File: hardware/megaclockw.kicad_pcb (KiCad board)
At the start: 2 copper layers, 26.8 x 65.5 mm, 3 parts, among them J1 Conn_01x08_Female, U1 74HC245

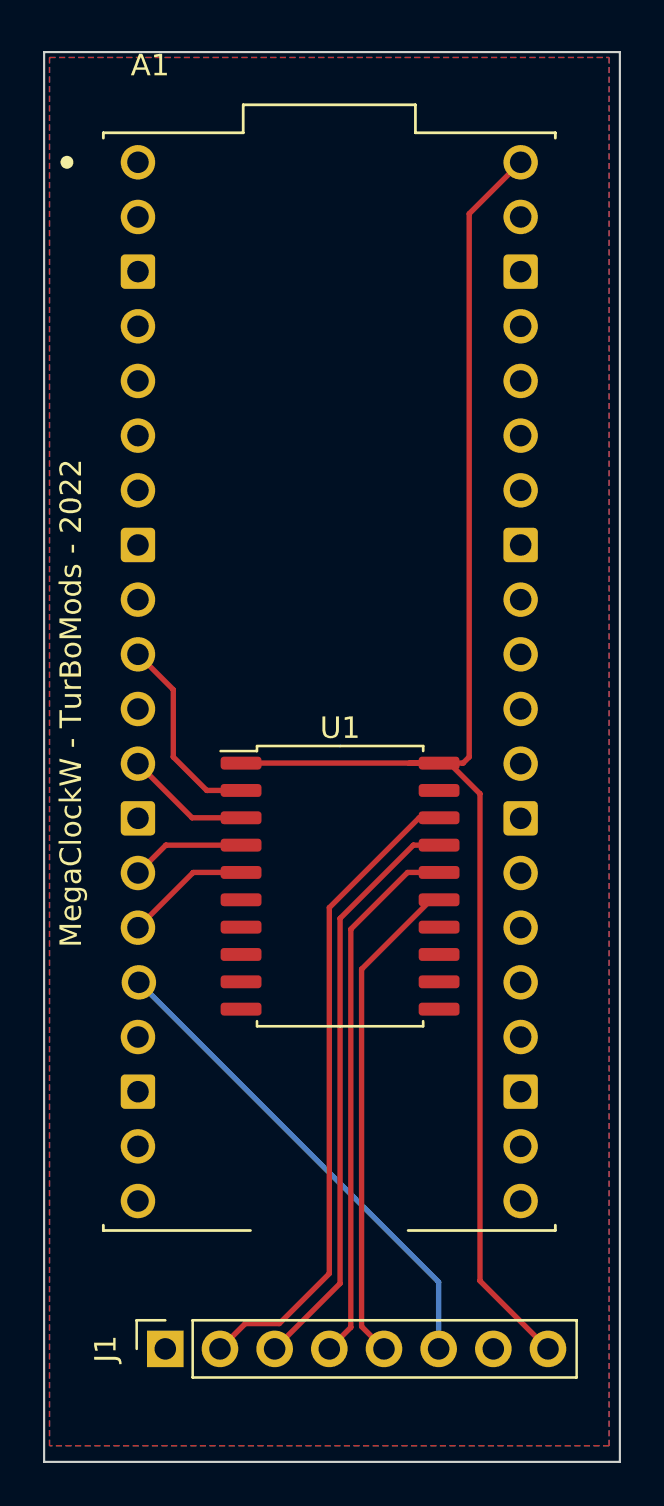
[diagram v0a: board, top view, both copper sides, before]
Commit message: better power lines
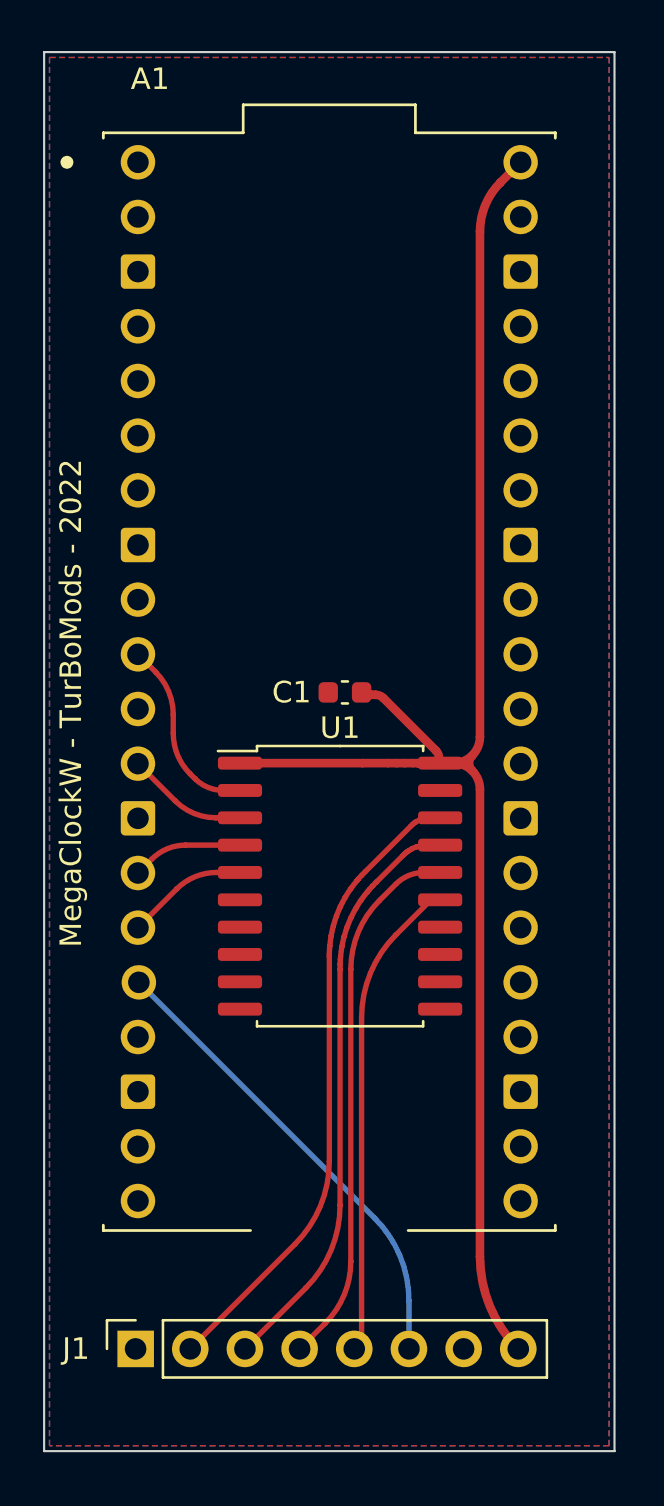
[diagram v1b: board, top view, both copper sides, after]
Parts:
- added C1: C_Small, Capacitor_SMD:C_0603_1608Metric, F.Cu at (182.7, 88.5)
- U1: footprint Package_SO:SOP-20_7.5x12.8mm_P1.27mm -> Package_SO:SOIC-20W_7.5x12.8mm_P1.27mm
- moved J1 1.38 mm to (173.0, 119.0)
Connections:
- A1 pad 16: unconnected-(A1-Pad16) -> /CPU_PWM
- J1 pad 7: unconnected-(J1-Pad7) -> GND
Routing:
- net +5V: track 70.4 -> 73.4 mm
- net /CPU_PIN_17: track 30.9 -> 29.0 mm
- net /CPU_PAUSE: track 9.19 -> 8.07 mm
- net /CPU_PWM: track 22.8 -> 22.0 mm
- net /JP3/4: track 25.2 -> 24.5 mm
- net /MD_RESET: track 27.3 -> 26.7 mm
- net /JP1/2: track 22.6 -> 22.1 mm
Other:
- board size 26.8 x 65.5 mm -> 26.5 x 65 mm
- board text added: "https://github.com/TurBoss/megaclockw"
